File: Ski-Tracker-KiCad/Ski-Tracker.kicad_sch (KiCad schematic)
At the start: 20 parts, among them J2 Conn_01x02_Pin, J3 Conn_01x05_Socket, SW1 SW_SPDT, U1 LSM6DSOXTR, U2 BMP388, U3 MCP73831T-2ACI/MC

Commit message: First time using copperPilot
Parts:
- added C5: 0.1uF, Capacitor_SMD:C_0402_1005Metric, symbol Device:C
- C3: value 0.1uF -> 4.7uF; footprint Capacitor_SMD:C_0402_1005Metric -> Capacitor_SMD:C_0805_2012Metric
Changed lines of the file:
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@@
+	(wire
+		(pts
+			(xy 245.11 30.48) (xy 251.46 30.48)
+		)
+		(stroke
+			(width 0)
+			(type default)
+		)
+	)
 	(wire
 		(pts
@@
 	(wire
 		(pts
-			(xy 255.27 30.48) (xy 251.46 30.48)
+			(xy 245.11 26.67) (xy 245.11 30.48)
 		)
 		(stroke
@@
 	(wire
 		(pts
-			(xy 217.17 72.39) (xy 218.44 72.39)
+			(xy 213.36 72.39) (xy 218.44 72.39)
 		)
 		(stroke
@@
 	)
 	(label "3V3"
-		(at 255.27 30.48 0)
+		(at 245.11 26.67 0)
 		(effects
 			(font
@@
 	)
 	(label "GND"
-		(at 217.17 72.39 0)
+		(at 213.36 72.39 0)
 		(effects
 			(font
@@
 			)
 		)
-		(property "Value" "0.1uF"
+		(property "Value" "4.7uF"
 			(at 84.836 120.65 90)
 			(effects
@@
 			)
 		)
-		(property "Footprint" "Capacitor_SMD:C_0402_1005Metric"
+		(property "Footprint" "Capacitor_SMD:C_0805_2012Metric"
 			(at 88.9 123.4948 0)
 			(effects
@@
 				(path "/be385fdf-30ca-4fee-90e6-af9ff65b4b39"
 					(reference "SW1")
+					(unit 1)
+				)
+			)
+		)
+	)
+	(symbol
+		(lib_id "Device:C")
+		(at 246.38 135.89 90)
+		(unit 1)
+		(exclude_from_sim no)
+		(in_bom yes)
+		(on_board yes)
+		(dnp no)
+		(property "Reference" "C5"
+			(at 246.38 128.524 90)
+			(effects
+				(font
+					(size 1.27 1.27)
+				)
+			)
+		)
+		(property "Value" "0.1uF"
+			(at 246.38 131.064 90)
+			(effects
+				(font
+					(size 1.27 1.27)
+				)
+			)
+		)
+		(property "Footprint" "Capacitor_SMD:C_0402_1005Metric"
+			(at 246.38 135.89 0)
+			(effects
+				(font
+					(size 1.27 1.27)
+				)
+				(hide yes)
+			)
+		)
+		(property "Datasheet" "~"
+			(at 246.38 135.89 0)
+			(effects
+				(font
+					(size 1.27 1.27)
+				)
+				(hide yes)
+			)
+		)
+		(property "Description" ""
+			(at 246.38 135.89 0)
+			(effects
+				(font
+					(size 1.27 1.27)
+				)
+				(hide yes)
+			)
+		)
+		(pin "1"
+		)
+		(pin "2"
+		)
+		(instances
+			(project "Ski-Tracker"
+				(path "/be385fdf-30ca-4fee-90e6-af9ff65b4b39"
+					(reference "C5")
 					(unit 1)
 				)
@@
 		(on_board yes)
 		(dnp no)
-		(fields_autoplaced yes)
 		(property "Reference" "#PWR01"
 			(at 251.46 31.75 0)
@@
 		)
 		(property "Value" "+3.3V"
-			(at 251.46 22.86 0)
-			(effects
-				(font
+			(at 245.872 20.828 0)
+			(effects
+				(font

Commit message: small changes
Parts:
- removed C5: 0.1uF, Capacitor_SMD:C_0402_1005Metric, symbol Device:C
- added D3, D4, D5: LED, LED_SMD:LED_0805_2012Metric, symbol Device:LED
- added R7, R8, R9: 220, Resistor_SMD:R_0603_1608Metric, symbol Device:R
- C6: footprint Capacitor_SMD:C_0402_1005Metric -> Capacitor_SMD:C_0805_2012Metric
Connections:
- net GND: now also D3.1 (K), D4.1 (K), D5.1 (K)
- net LED1: now reaches A1.24 (GPIO18)
- net LED1: now also R7.1
- net LED2: now reaches A1.25 (GPIO19)
- net LED2: now also R8.1
- net LED3: now reaches A1.26 (GPIO20)
- net LED3: now also R9.1
- new net: D4.2 (A), R8.2
- new net: D5.2 (A), R9.2
- new net: D3.2 (A), R7.2
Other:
- note added: "Status LED"

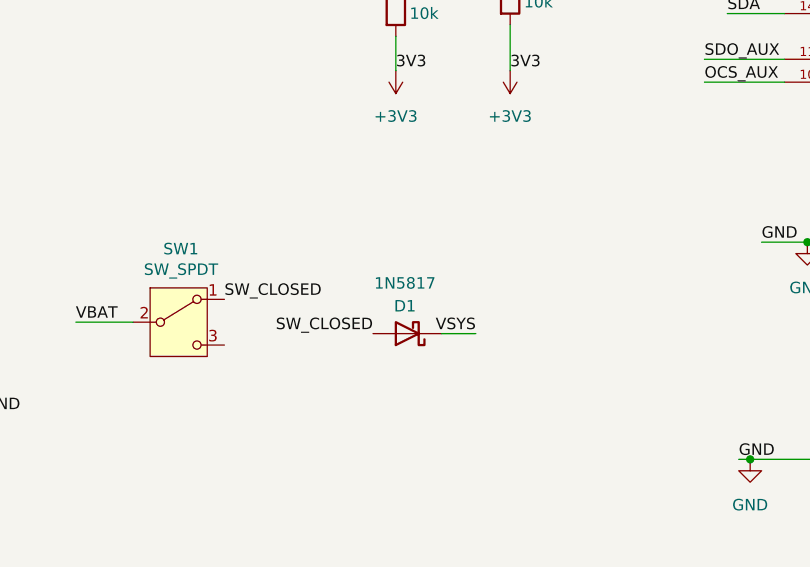
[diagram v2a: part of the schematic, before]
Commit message: changed diode value
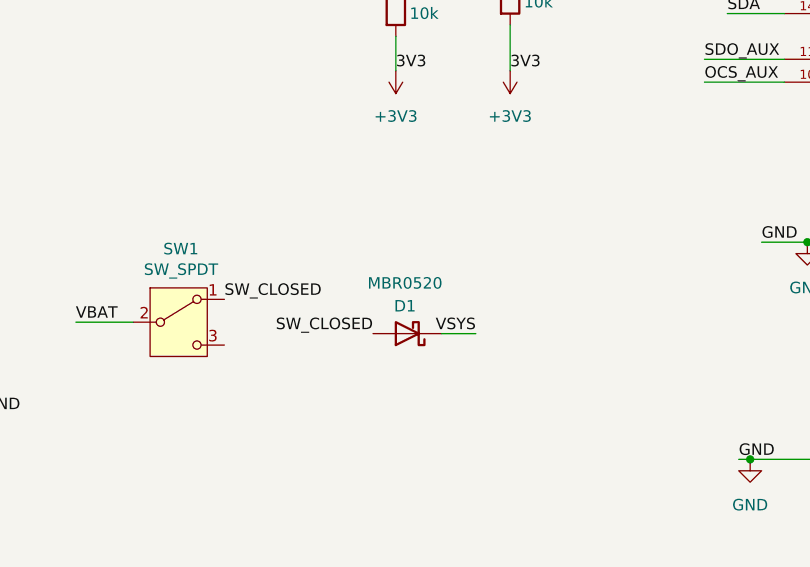
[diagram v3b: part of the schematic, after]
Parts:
- D1: value 1N5817 -> MBR0520
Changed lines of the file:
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@@
 			)
 		)
-		(property "Value" "1N5817"
+		(property "Value" "MBR0520"
 			(at 173.736 76.962 0)
 			(effects

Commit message: Status LED
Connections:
- net +3.3V renamed +3V3

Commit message: KiCad 10 update
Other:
- moved on the sheet: C1
